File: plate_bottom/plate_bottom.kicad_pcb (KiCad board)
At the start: 2 copper layers, 180.6 x 117.9 mm, 12 parts

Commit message: Minor changes
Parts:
- added HM13: CaseHole, used_footprints:M2_HOLE_PCB, F.Cu at (154.6, 116.2)
- moved HM4 11.1 mm to (186.0, 112.9)
- moved HM1 3.76 mm to (224.9, 122.5)
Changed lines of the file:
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@@
     (tracks 0)
     (zones 0)
-    (modules 12)
+    (modules 13)
     (nets 1)
   )
@@
   )
   (module used_footprints:M2_HOLE_PCB (layer F.Cu)
+    (at 185.99 112.92)
+    (fp_text reference HM4 (at 0 2.7) (layer F.SilkS) hide
+      (effects (font (size 1 1) (thickness 0.15)))
+    )
+    (fp_text value CaseHole (at 0 -2.6) (layer F.Fab) hide
+      (effects (font (size 1 1) (thickness 0.15)))
+    )
+    (pad "" thru_hole circle (at 0 0) (size 4 4) (drill 2.2) (layers *.Cu *.Mask))
+  )
+  (module used_footprints:M2_HOLE_PCB (layer F.Cu)
+    (at 224.86 122.47)
+    (fp_text reference HM1 (at 0 2.7) (layer F.SilkS) hide
+      (effects (font (size 1 1) (thickness 0.15)))
+    )
+    (fp_text value CaseHole (at 0 -2.6) (layer F.Fab) hide
+      (effects (font (size 1 1) (thickness 0.15)))
+    )
+    (pad "" thru_hole circle (at 0 0) (size 4 4) (drill 2.2) (layers *.Cu *.Mask))
+  )
+  (module used_footprints:M2_HOLE_PCB (layer F.Cu)
+    (at 154.63 116.15)
+    (fp_text reference HM13 (at 0 2.7) (layer F.SilkS) hide
+      (effects (font (size 1 1) (thickness 0.15)))
+    )
+    (fp_text value CaseHole (at 0 -2.6) (layer F.Fab) hide
+      (effects (font (size 1 1) (thickness 0.15)))
+    )
+    (pad "" thru_hole circle (at 0 0) (size 4 4) (drill 2.2) (layers *.Cu *.Mask))
+  )
+  (module used_footprints:M2_HOLE_PCB (layer F.Cu)
     (at 222.15 72.61)
     (fp_text reference H16 (at 0 2.7) (layer F.SilkS) hide
@@
     )
     (fp_text value MountingHole (at 0 -2.6) (layer F.Fab) hide
-      (effects (font (size 1 1) (thickness 0.15)))
-    )
-    (pad "" thru_hole circle (at 0 0) (size 4 4) (drill 2.2) (layers *.Cu *.Mask))
-  )
-  (module used_footprints:M2_HOLE_PCB (layer F.Cu)
-    (at 221.15 123.1)
-    (fp_text reference HM1 (at 0 2.7) (layer F.SilkS) hide
-      (effects (font (size 1 1) (thickness 0.15)))
-    )
-    (fp_text value CaseHole (at 0 -2.6) (layer F.Fab) hide
       (effects (font (size 1 1) (thickness 0.15)))
     )
@@
       (effects (font (size 1 1) (thickness 0.15)))
     )
-    (fp_text value CaseHole (at 0 -2.6) (layer F.Fab) hide
-      (effects (font (size 1 1) (thickness 0.15)))
-    )
-    (pad "" thru_hole circle (at 0 0) (size 4 4) (drill 2.2) (layers *.Cu *.Mask))
-  )
-  (module used_footprints:M2_HOLE_PCB (layer F.Cu)
-    (at 175.14 115.3)
-    (fp_text reference HM4 (at 0 2.7) (layer F.SilkS) hide
-      (effects (font (size 1 1) (thickness 0.15)))
-    )

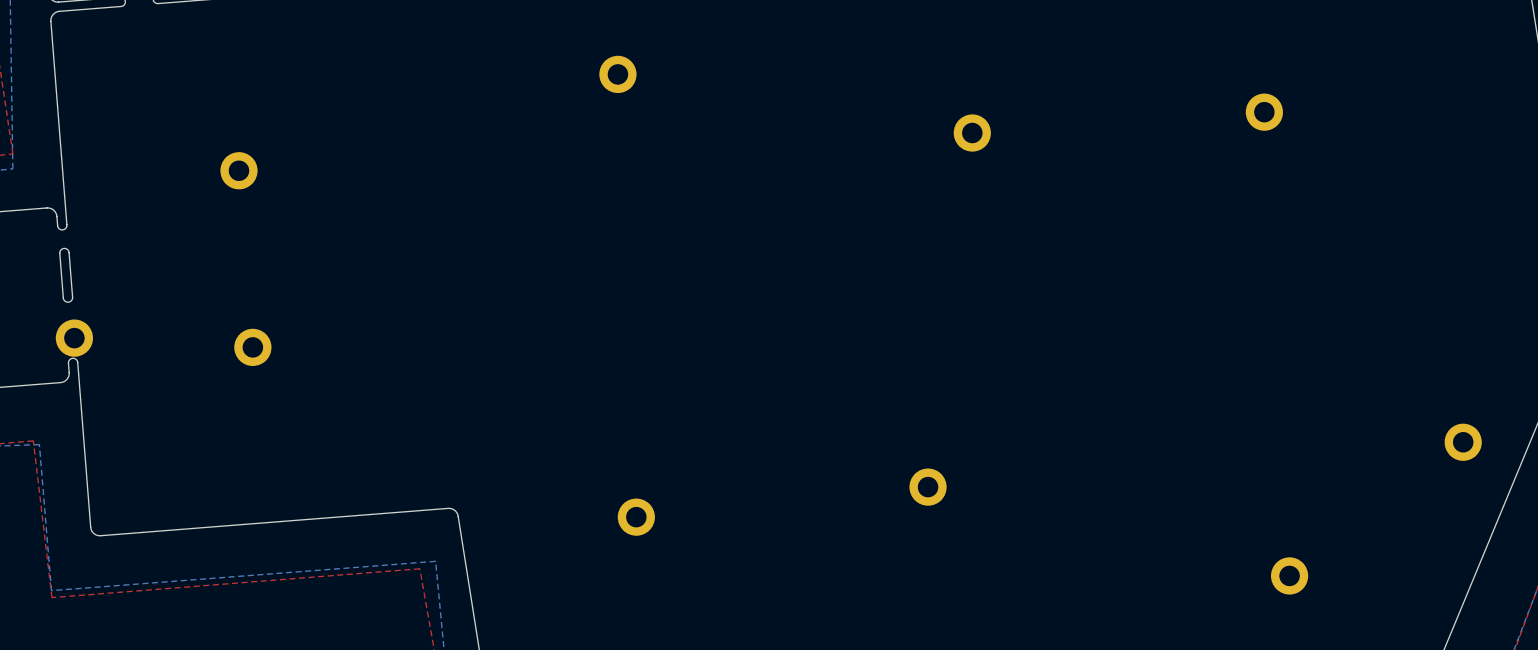
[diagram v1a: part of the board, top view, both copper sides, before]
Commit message: Changed holes a bit. Removed old gerbers.
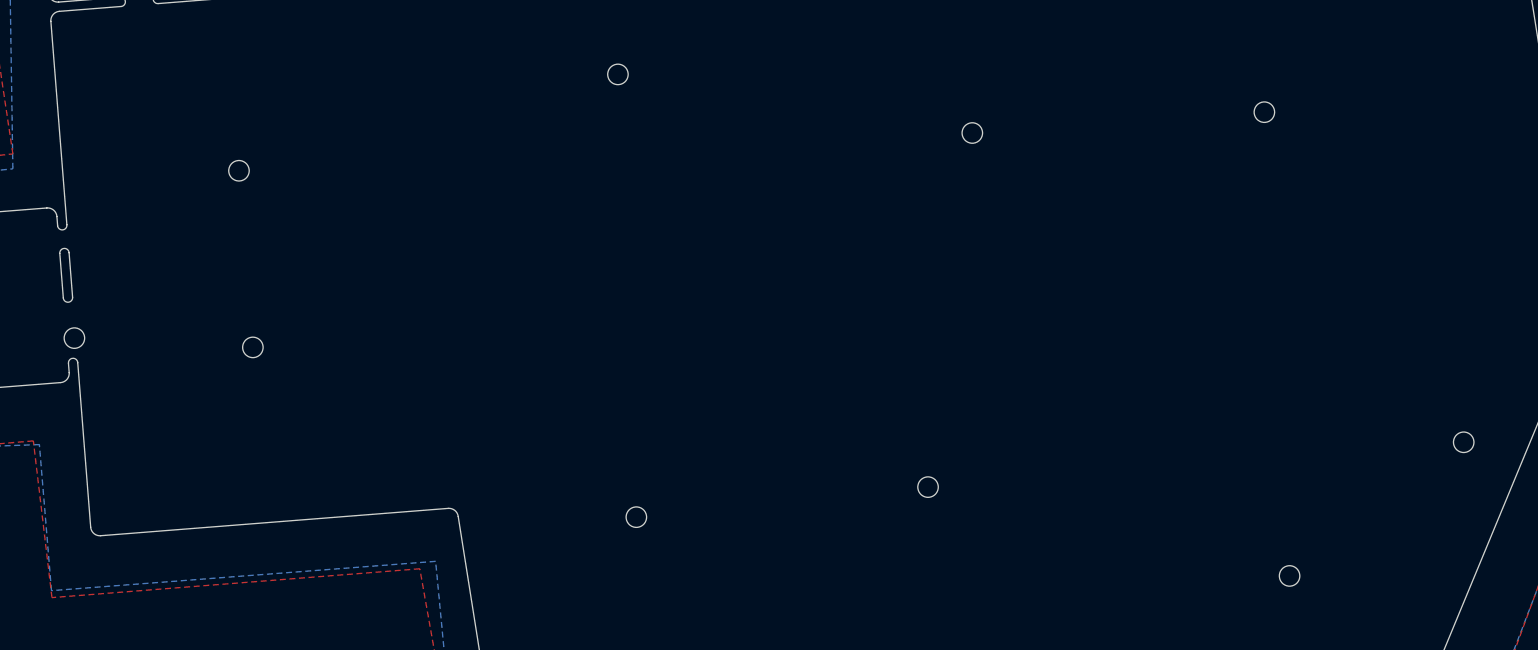
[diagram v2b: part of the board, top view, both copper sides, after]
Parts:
- moved HM3 0.05 mm to (243.6, 108.1)
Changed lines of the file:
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@@
+  )
+  (module used_footprints:M2_HOLE_PCB (layer F.Cu)
+    (at 154.63 116.15)
+    (fp_text reference HM13 (at 0 2.7) (layer F.SilkS) hide
+      (effects (font (size 1 1) (thickness 0.15)))
+    )
+    (fp_text value CaseHole (at 0 -2.6) (layer F.Fab) hide
+      (effects (font (size 1 1) (thickness 0.15)))
+    )
+    (pad "" np_thru_hole circle (at 0 0) (size 2.2 2.2) (drill 2.2) (layers *.Cu *.Mask))
+  )
+  (module used_footprints:M2_HOLE_PCB (layer F.Cu)
+    (at 222.15 72.61)
+    (fp_text reference H16 (at 0 2.7) (layer F.SilkS) hide
+      (effects (font (size 1 1) (thickness 0.15)))
+    )
+    (fp_text value MountingHole (at 0 -2.6) (layer F.Fab) hide
+      (effects (font (size 1 1) (thickness 0.15)))
+    )
+    (pad "" np_thru_hole circle (at 0 0) (size 2.2 2.2) (drill 2.2) (layers *.Cu *.Mask))
+  )
+  (module used_footprints:M2_HOLE_PCB (layer F.Cu)
+    (at 224.86 122.47)
+    (fp_text reference HM1 (at 0 2.7) (layer F.SilkS) hide
+      (effects (font (size 1 1) (thickness 0.15)))
+    )
+    (fp_text value CaseHole (at 0 -2.6) (layer F.Fab) hide
+      (effects (font (size 1 1) (thickness 0.15)))
+    )
+    (pad "" np_thru_hole circle (at 0 0) (size 2.2 2.2) (drill 2.2) (layers *.Cu *.Mask))
+  )
+  (module used_footprints:M2_HOLE_PCB (layer F.Cu)
+    (at 243.58032 108.09873)
+    (fp_text reference HM3 (at 0 2.7) (layer F.SilkS) hide
+      (effects (font (size 1 1) (thickness 0.15)))
+    )
+    (fp_text value CaseHole (at 0 -2.6) (layer F.Fab) hide
+      (effects (font (size 1 1) (thickness 0.15)))
+    )
+    (pad "" np_thru_hole circle (at 0 0) (size 2.2 2.2) (drill 2.2) (layers *.Cu *.Mask))
   )
   (module used_footprints:M2_HOLE_PCB (layer F.Cu)
@@
       (effects (font (size 1 1) (thickness 0.15)))
     )
-    (pad "" thru_hole circle (at 0 0) (size 4 4) (drill 2.2) (layers *.Cu *.Mask))
-  )
-  (module used_footprints:M2_HOLE_PCB (layer F.Cu)
-    (at 224.86 122.47)
-    (fp_text reference HM1 (at 0 2.7) (layer F.SilkS) hide
-      (effects (font (size 1 1) (thickness 0.15)))
-    )
-    (fp_text value CaseHole (at 0 -2.6) (layer F.Fab) hide
-      (effects (font (size 1 1) (thickness 0.15)))
-    )
-    (pad "" thru_hole circle (at 0 0) (size 4 4) (drill 2.2) (layers *.Cu *.Mask))
-  )
-  (module used_footprints:M2_HOLE_PCB (layer F.Cu)
-    (at 154.63 116.15)
-    (fp_text reference HM13 (at 0 2.7) (layer F.SilkS) hide
-      (effects (font (size 1 1) (thickness 0.15)))
-    )
-    (fp_text value CaseHole (at 0 -2.6) (layer F.Fab) hide
-      (effects (font (size 1 1) (thickness 0.15)))
-    )
-    (pad "" thru_hole circle (at 0 0) (size 4 4) (drill 2.2) (layers *.Cu *.Mask))
-  )
-  (module used_footprints:M2_HOLE_PCB (layer F.Cu)
-    (at 222.15 72.61)
-    (fp_text reference H16 (at 0 2.7) (layer F.SilkS) hide
-      (effects (font (size 1 1) (thickness 0.15)))
-    )
-    (fp_text value MountingHole (at 0 -2.6) (layer F.Fab) hide
-      (effects (font (size 1 1) (thickness 0.15)))
-    )
-    (pad "" thru_hole circle (at 0 0) (size 4 4) (drill 2.2) (layers *.Cu *.Mask))
-  )
-  (module used_footprints:M2_HOLE_PCB (layer F.Cu)
-    (at 191.3 55.15 14.5)
-    (fp_text reference HM2 (at 0 2.7 14.5) (layer F.SilkS) hide
-      (effects (font (size 1 1) (thickness 0.15)))
-    )
-    (fp_text value CaseHole (at 0 -2.6 14.5) (layer F.Fab) hide
-      (effects (font (size 1 1) (thickness 0.15)))
-    )
-    (pad "" np_thru_hole circle (at 0 0 14.5) (size 2.2 2.2) (drill 2.2) (layers *.Cu *.Mask))
-  )
-  (module used_footprints:M2_HOLE_PCB (layer F.Cu)
-    (at 243.526909 108.098711)
-    (fp_text reference HM3 (at 0 2.7) (layer F.SilkS) hide
-      (effects (font (size 1 1) (thickness 0.15)))
-    )
-    (fp_text value CaseHole (at 0 -2.6) (layer F.Fab) hide
-      (effects (font (size 1 1) (thickness 0.15)))
-    )
-    (pad "" thru_hole circle (at 0 0) (size 4 4) (drill 2.2) (layers *.Cu *.Mask))
+    (pad "" np_thru_hole circle (at 0 0) (size 2.2 2.2) (drill 2.2) (layers *.Cu *.Mask))
   )
   (module used_footprints:M2_HOLE_PCB (layer F.Cu)
@@
       (effects (font (size 1 1) (thickness 0.15)))
     )
-    (pad "" thru_hole circle (at 0 0 4.5) (size 4 4) (drill 2.2) (layers *.Cu *.Mask))
+    (pad "" np_thru_hole circle (at 0 0 4.5) (size 2.2 2.2) (drill 2.2) (layers *.Cu *.Mask))
   )
   (module used_footprints:M2_HOLE_PCB (layer F.Cu)
     (at 113.402232 97.899367 4.5)
     (fp_text reference HM6 (at 0 2.7 4.5) (layer F.SilkS) hide
-      (effects (font (size 1 1) (thickness 0.15)))
-    )
-    (fp_text value CaseHole (at 0 -2.6 4.5) (layer F.Fab) hide
-      (effects (font (size 1 1) (thickness 0.15)))
-    )
-    (pad "" thru_hole circle (at 0 0 4.5) (size 4 4) (drill 2.2) (layers *.Cu *.Mask))
-  )
-  (module used_footprints:M2_HOLE_PCB (layer F.Cu)
-    (at 110.411788 59.264897 4.5)
-    (fp_text reference HM7 (at 0 2.7 4.5) (layer F.SilkS) hide
       (effects (font (size 1 1) (thickness 0.15)))
     )
@@
       (effects (font (size 1 1) (thickness 0.15)))
     )
-    (pad "" thru_hole circle (at 0 0 4.5) (size 4 4) (drill 2.2) (layers *.Cu *.Mask))
+    (pad "" np_thru_hole circle (at 0 0 4.5) (size 2.2 2.2) (drill 2.2) (layers *.Cu *.Mask))
+  )
+  (module used_footprints:M2_HOLE_PCB (layer F.Cu)
+    (at 190.75 74.85)
+    (fp_text reference HM10 (at 0 2.7) (layer F.SilkS) hide
+      (effects (font (size 1 1) (thickness 0.15)))
+    )
+    (fp_text value CaseHole (at 0 -2.6) (layer F.Fab) hide
+      (effects (font (size 1 1) (thickness 0.15)))
+    )
+    (pad "" np_thru_hole circle (at 0 0) (size 2.2 2.2) (drill 2.2) (layers *.Cu *.Mask))
+  )
+  (module used_footprints:M2_HOLE_PCB (layer F.Cu)
+    (at 152.65 68.55)
+    (fp_text reference HM11 (at 0 2.7) (layer F.SilkS) hide
+      (effects (font (size 1 1) (thickness 0.15)))
+    )
+    (fp_text value CaseHole (at 0 -2.6) (layer F.Fab) hide
+      (effects (font (size 1 1) (thickness 0.15)))
+    )
+    (pad "" np_thru_hole circle (at 0 0) (size 2.2 2.2) (drill 2.2) (layers *.Cu *.Mask))
+  )
+  (module used_footprints:M2_HOLE_PCB (layer F.Cu)
+    (at 191.3 55.15 14.5)
+    (fp_text reference HM2 (at 0 2.7 14.5) (layer F.SilkS) hide
+      (effects (font (size 1 1) (thickness 0.15)))
+    )
+    (fp_text value CaseHole (at 0 -2.6 14.5) (layer F.Fab) hide
+      (effects (font (size 1 1) (thickness 0.15)))
+    )
+    (pad "" np_thru_hole circle (at 0 0 14.5) (size 2.2 2.2) (drill 2.2) (layers *.Cu *.Mask))
+  )
+  (module used_footprints:M2_HOLE_PCB (layer F.Cu)
+    (at 110.411788 59.264897 4.5)
+    (fp_text reference HM7 (at 0 2.7 4.5) (layer F.SilkS) hide
+      (effects (font (size 1 1) (thickness 0.15)))
+    )
+    (fp_text value CaseHole (at 0 -2.6 4.5) (layer F.Fab) hide
+      (effects (font (size 1 1) (thickness 0.15)))
+    )
+    (pad "" np_thru_hole circle (at 0 0 4.5) (size 2.2 2.2) (drill 2.2) (layers *.Cu *.Mask))
   )
   (module used_footprints:M2_HOLE_PCB (layer F.Cu)
@@
     (pad "" np_thru_hole circle (at 0 0) (size 2.2 2.2) (drill 2.2) (layers *.Cu *.Mask))
   )
-  (module used_footprints:M2_HOLE_PCB (layer F.Cu)
-    (at 190.75 74.85)
-    (fp_text reference HM10 (at 0 2.7) (layer F.SilkS) hide
-      (effects (font (size 1 1) (thickness 0.15)))
-    )
-    (fp_text value CaseHole (at 0 -2.6) (layer F.Fab) hide
-      (effects (font (size 1 1) (thickness 0.15)))
-    )
-    (pad "" thru_hole circle (at 0 0) (size 4 4) (drill 2.2) (layers *.Cu *.Mask))
-  )
-  (module used_footprints:M2_HOLE_PCB (layer F.Cu)
-    (at 152.65 68.55)
-    (fp_text reference HM11 (at 0 2.7) (layer F.SilkS) hide
-      (effects (font (size 1 1) (thickness 0.15)))
-    )
-    (fp_text value CaseHole (at 0 -2.6) (layer F.Fab) hide
-      (effects (font (size 1 1) (thickness 0.15)))
-    )
-    (pad "" thru_hole circle (at 0 0) (size 4 4) (drill 2.2) (layers *.Cu *.Mask))
-  )
   (dimension 180.65 (width 0.15) (layer Dwgs.User)
